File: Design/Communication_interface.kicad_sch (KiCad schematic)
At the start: 6 parts

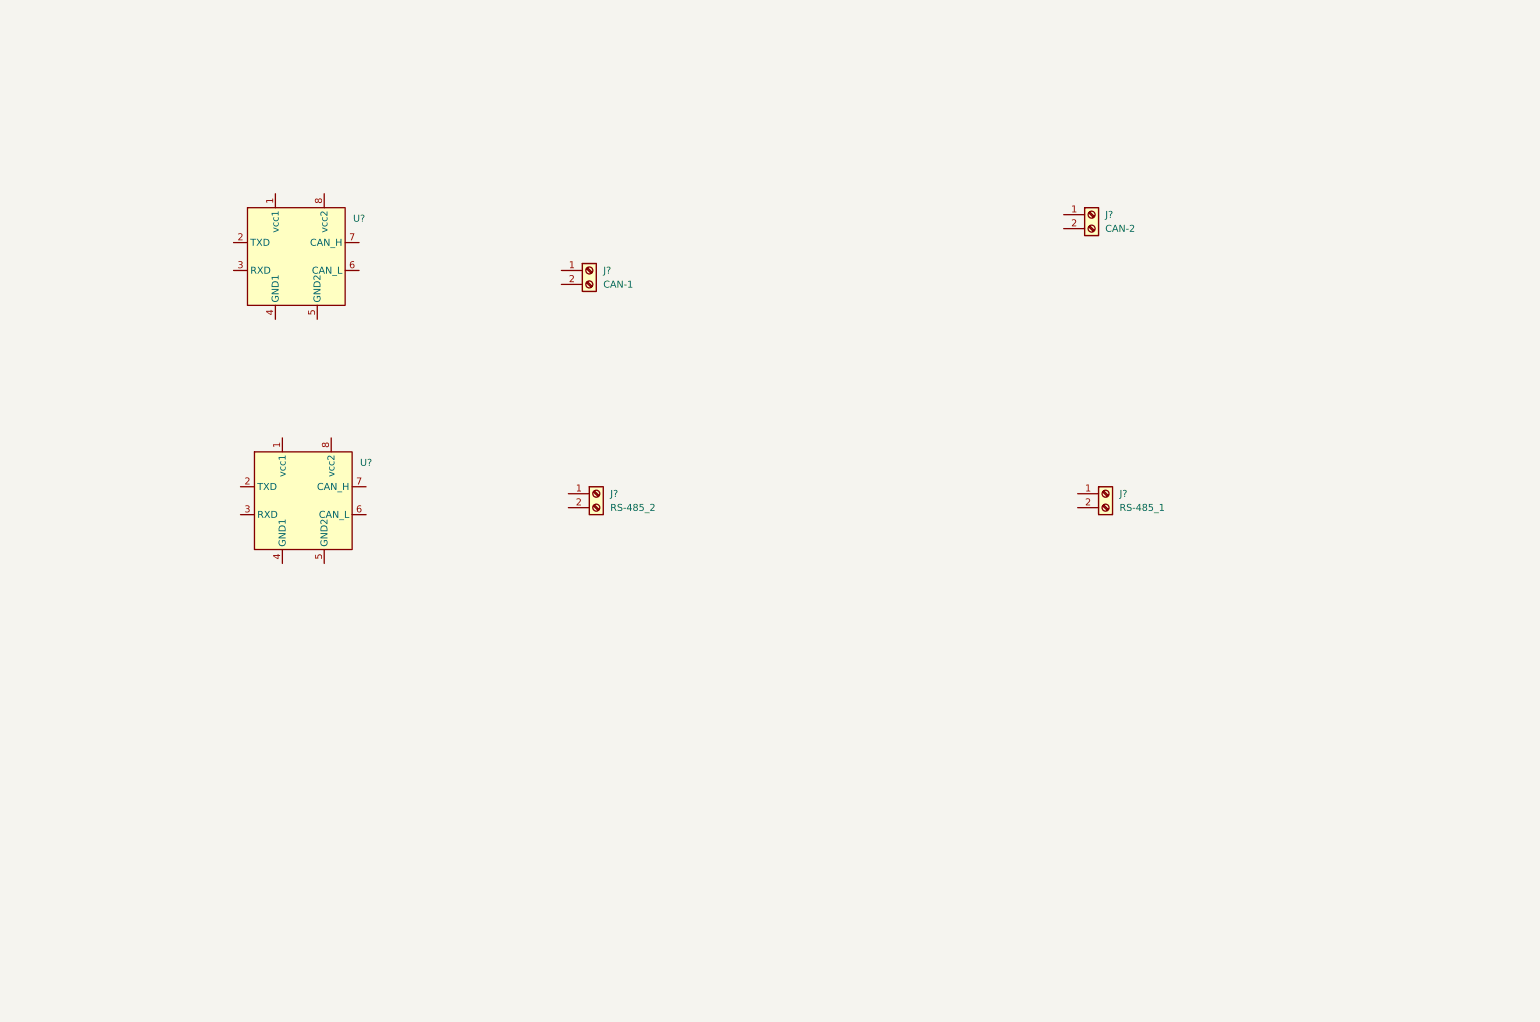
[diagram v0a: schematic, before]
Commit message: Added Comps in Communication.sch
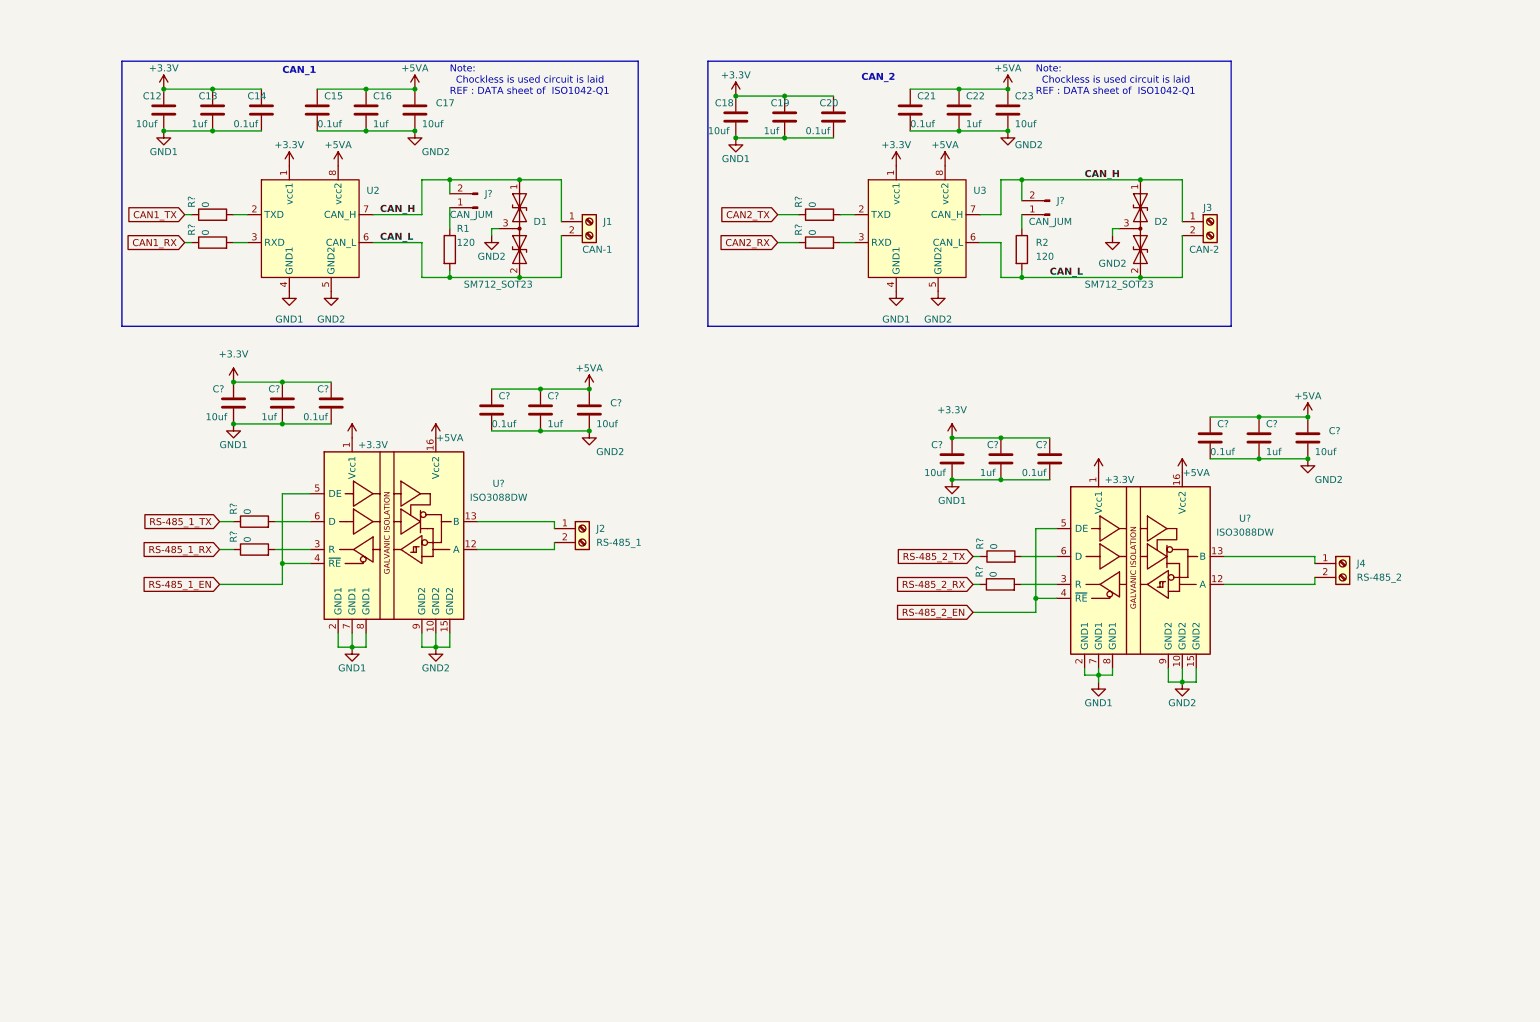
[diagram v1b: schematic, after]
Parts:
- added C12, C17, C18, C23, C? (x4): 10uf, symbol Device:C
- added C13, C16, C19, C22, C? (x4): 1uf, symbol Device:C
- added C14, C15, C20, C21, C? (x4): 0.1uf, symbol Device:C
- added D1, D2: SM712_SOT23, Package_TO_SOT_SMD:SOT-23, symbol Diode:SM712_SOT23
- added J? (x2): CAN_JUM, symbol Connector:Conn_01x02_Pin
- added R1, R2: 120, symbol Device:R
- added R? (x8): 0, symbol Device:R
- added U? (x2): ISO3088DW, Package_SO:SOIC-16W_7.5x10.3mm_P1.27mm, symbol Interface_UART:ISO3088DW
- gave numbers to parts that had none: 6
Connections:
- net CAN_H: now reaches J1.1 (Pin_1)
- net CAN_H: now also J3.1 (Pin_1), U2.7 (CAN_H), U3.7 (CAN_H), D1.1 (A1), D2.1 (A1), J?.2 (Pin_2), J?.2 (Pin_2)
- net CAN_L: now reaches J1.2 (Pin_2)
- net CAN_L: now also J3.2 (Pin_2), U2.6 (CAN_L), U3.6 (CAN_L), D1.2 (A2), D2.2 (A2), R1.2, R2.2
- net +3.3V: now reaches U2.1 (vcc1)
- net +3.3V: now also U3.1 (vcc1), C12.1, C13.1, C14.2, C18.1, C19.1, C20.2, C?.1, C?.1, C?.1, C?.1, C?.2, C?.2, U?.1 (Vcc1), U?.1 (Vcc1)
- net at U2.2 (TXD): now also R?.2
- net at U2.3 (RXD): now also R?.2
- net GND1: now reaches U2.4 (GND1)
- net GND1: now also U3.4 (GND1), C12.2, C13.2, C14.1, C18.2, C19.2, C20.1, C?.1, C?.1, C?.2, C?.2, C?.2, C?.2, U?.2 (GND1), U?.2 (GND1), U?.7 (GND1), U?.7 (GND1), U?.8 (GND1), U?.8 (GND1)
- net GND2: now reaches U2.5 (GND2)
- net GND2: now also U3.5 (GND2), C15.2, C16.2, C17.1, C21.2, C22.2, C23.1, C?.1, C?.1, C?.2, C?.2, C?.2, C?.2, D1.3 (common), D2.3 (common), U?.10 (GND2), U?.10 (GND2), U?.15 (GND2), U?.15 (GND2), U?.9 (GND2), U?.9 (GND2)
- net +5VA: now reaches U2.8 (vcc2)
- net +5VA: now also U3.8 (vcc2), C15.1, C16.1, C17.2, C21.1, C22.1, C23.2, C?.1, C?.1, C?.1, C?.1, C?.2, C?.2, U?.16 (Vcc2), U?.16 (Vcc2)
- net at U3.2 (TXD): now also R?.2
- net at U3.3 (RXD): now also R?.2
- net at J4.1 (Pin_1): now also U?.13 (B)
- net at J4.2 (Pin_2): now also U?.12 (A)
- net at J2.1 (Pin_1): now also U?.13 (B)
- net at J2.2 (Pin_2): now also U?.12 (A)
- new net: J?.1 (Pin_1), R2.1
- new net: R?.2, U?.3 (R) (x2)
- new net: R?.2, U?.6 (D) (x2)
- new net: J?.1 (Pin_1), R1.1
- new net CAN1_RX: R?.1
- new net CAN1_TX: R?.1
- new net CAN2_RX: R?.1
- new net CAN2_TX: R?.1
- new net RS-485_1_EN: U?.4 (~{RE}), U?.5 (DE)
- new net RS-485_1_RX: R?.1
- new net RS-485_1_TX: R?.1
- new net RS-485_2_EN: U?.4 (~{RE}), U?.5 (DE)
- new net RS-485_2_RX: R?.1
- new net RS-485_2_TX: R?.1
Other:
- note added: "CAN_1"
- note added: "CAN_2"
- note added: "Note: Chockless is used circuit is laid REF : DATA sheet of ISO1042-Q1"
- moved on the sheet: J1, J2, J3, J4, U2, U3

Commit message: Added reference file for chokless CAN and DC-DC converter in main sch
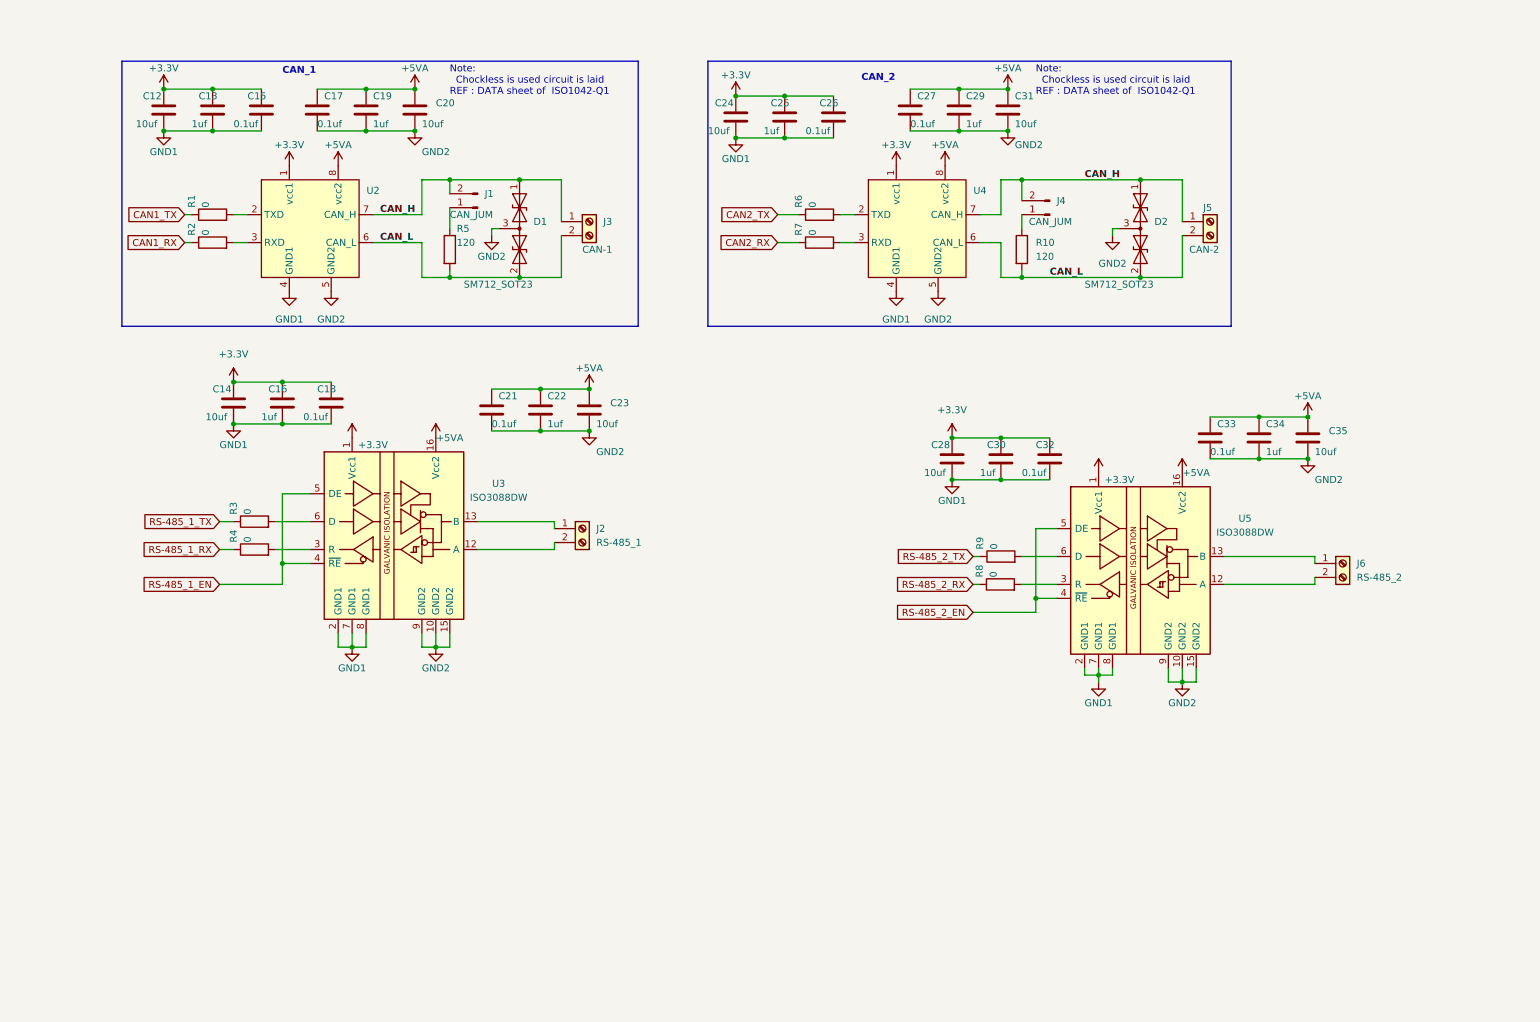
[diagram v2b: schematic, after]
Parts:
- gave numbers to parts that had none: 24
- renumbered C14 to C15, C15 to C17, C16 to C19, C17 to C20, C18 to C24, C19 to C25, C20 to C26, C21 to C27, C22 to C29, C23 to C31, J1 to J3, J3 to J5, J4 to J6, R2 to R10, R1 to R5, U3 to U4

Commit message: Communication.sch modified , 75% finished
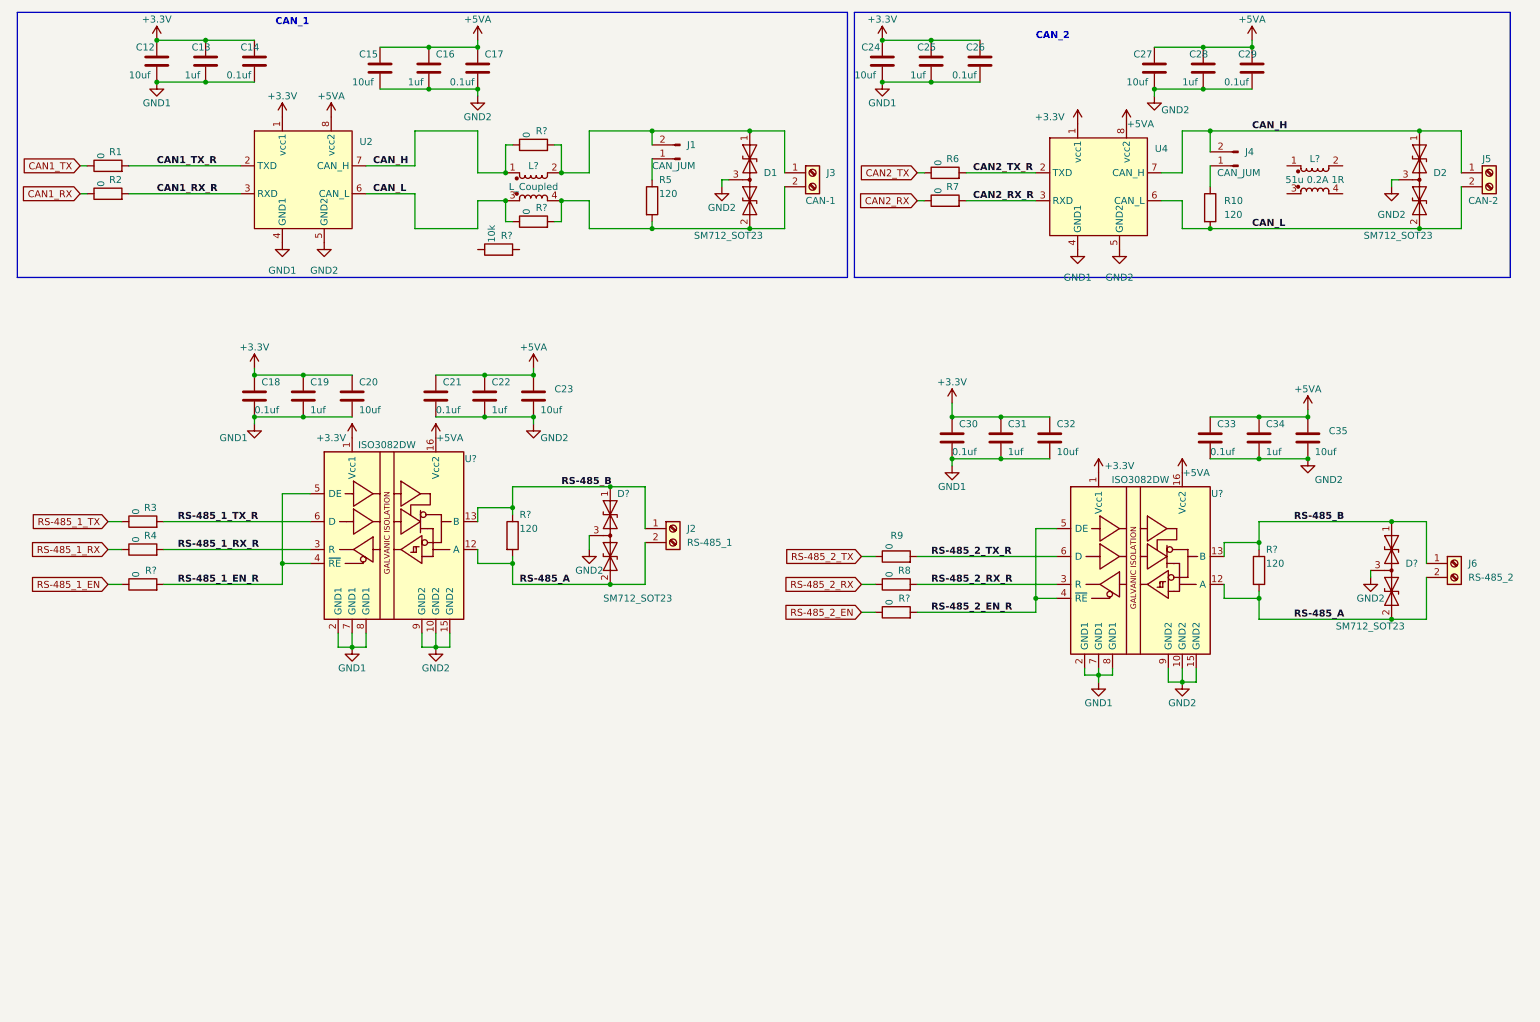
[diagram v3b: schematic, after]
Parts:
- removed U3, U5: ISO3088DW, Package_SO:SOIC-16W_7.5x10.3mm_P1.27mm, symbol Interface_UART:ISO3088DW
- added D? (x2): SM712_SOT23, Package_TO_SOT_SMD:SOT-23, symbol Diode:SM712_SOT23
- added L?: L_Coupled, symbol Device:L_Coupled
- added L?: 51u 0.2A 1R, symbol Device:L_Coupled
- added R? (x2): 120, symbol Device:R
- added R? (x4): 0, symbol Device:R
- added R?: 10k, symbol Device:R
- added U? (x2): ISO3082DW, Package_SO:SOIC-16W_7.5x10.3mm_P1.27mm, symbol Interface_UART:ISO3082DW
- renumbered C15 to C14, C14 to C15, C18 to C17, C17 to C18, C28 to C27, C30 to C28, C32 to C29, C27 to C30, C29 to C31, C31 to C32
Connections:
- net +3.3V: now also C18.1, C19.1, C20.2, C30.1, C31.1, C32.2, U?.1 (Vcc1), U?.1 (Vcc1); no longer C15.1, C16.1, C17.2, C27.1, C28.1, C29.2
- net +5VA: now also C15.1, C16.1, C17.2, C27.1, C28.1, C29.2, U?.16 (Vcc2), U?.16 (Vcc2); no longer C18.1, C19.1, C20.2, C30.1, C31.1, C32.2
- net CAN_H: now also L?.1, R?.1; no longer D1.1 (A1), J1.2 (Pin_2), J3.1 (Pin_1)
- net CAN_L: now also L?.3, R?.1; no longer D1.2 (A2), J3.2 (Pin_2), R5.2
- net GND1: now also C18.2, C19.2, C20.1, C30.2, C31.2, C32.1, U?.2 (GND1), U?.2 (GND1), U?.7 (GND1), U?.7 (GND1), U?.8 (GND1), U?.8 (GND1); no longer C15.2, C16.2, C17.1, C27.2, C28.2, C29.1
- net GND2: now also C15.2, C16.2, C17.1, C27.2, C28.2, C29.1, D?.3 (common), D?.3 (common), U?.10 (GND2), U?.10 (GND2), U?.15 (GND2), U?.15 (GND2), U?.9 (GND2), U?.9 (GND2); no longer C18.2, C19.2, C20.1, C30.2, C31.2, C32.1
- net RS-485_1_EN: now also R?.1
- net RS-485_2_EN: now also R?.1
- net RS-485_2_RX_R: now reaches R8.2
- net RS-485_2_RX_R: now also U?.3 (R)
- net CAN1_RX_R: now reaches R2.2, U2.3 (RXD)
- net RS-485_1_TX_R: now reaches R3.2
- net RS-485_1_TX_R: now also U?.6 (D)
- net RS-485_A: now reaches J6.2 (Pin_2)
- net RS-485_A: now also J2.2 (Pin_2), D?.2 (A2), D?.2 (A2), R?.2, R?.2, U?.12 (A), U?.12 (A)
- net RS-485_B: now reaches J6.1 (Pin_1)
- net RS-485_B: now also J2.1 (Pin_1), D?.1 (A1), D?.1 (A1), R?.1, R?.1, U?.13 (B), U?.13 (B)
- net RS-485_2_TX_R: now reaches R9.2
- net RS-485_2_TX_R: now also U?.6 (D)
- net CAN2_TX_R: now reaches R6.2, U4.2 (TXD)
- net CAN1_TX_R: now reaches R1.2, U2.2 (TXD)
- net CAN2_RX_R: now reaches R7.2, U4.3 (RXD)
- net RS-485_1_RX_R: now reaches R4.2
- net RS-485_1_RX_R: now also U?.3 (R)
- new net: D1.1 (A1), J1.2 (Pin_2), J3.1 (Pin_1), L?.2, R?.2
- new net: D1.2 (A2), J3.2 (Pin_2), L?.4, R5.2, R?.2
- new net RS-485_1_EN_R: R?.2, U?.4 (~{RE}), U?.5 (DE)
- new net RS-485_2_EN_R: R?.2, U?.4 (~{RE}), U?.5 (DE)
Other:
- note removed: "Note: Chockless is used circuit is laid REF : DATA sheet of ISO1042-Q1"
- moved on the sheet: C12, C13, C14, C15, C16, C17, C18, C19, C20, C21, C22, C23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

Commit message: Added HUM and TEMP sense
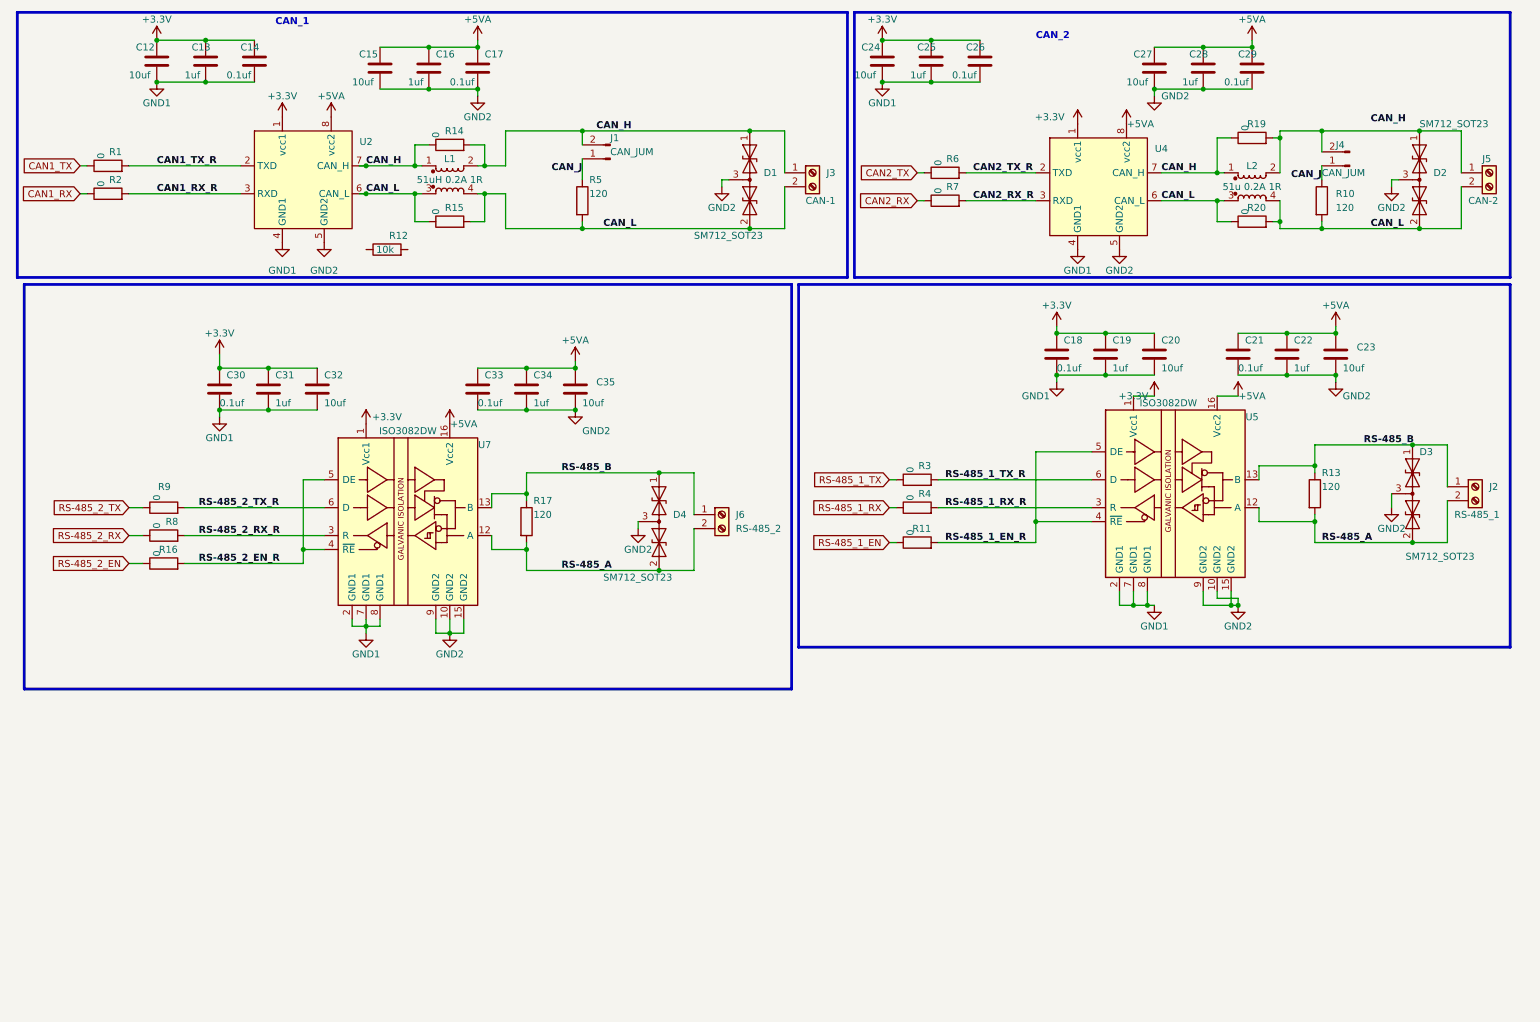
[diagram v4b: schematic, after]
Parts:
- added R19, R20: 0, symbol Device:R
- L1: renamed from L?; value L_Coupled -> 51uH 0.2A 1R
- gave numbers to parts that had none: 12
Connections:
- net CAN_H: now also D1.1 (A1), J1.2 (Pin_2), J3.1 (Pin_1), L1.2, L2.1, R14.2, R19.1; no longer D2.1 (A1), J4.2 (Pin_2), J5.1 (Pin_1)
- net CAN_L: now also D1.2 (A2), J3.2 (Pin_2), L1.4, L2.3, L2.4, R15.2, R5.2, R20.1, R20.2
- net CAN_J: now reaches J4.1 (Pin_1), R10.1
- net CAN_J: now also J1.1 (Pin_1), R5.1
- net at L2.2: now also D2.1 (A1), J4.2 (Pin_2), J5.1 (Pin_1), R19.2
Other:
- moved on the sheet: C18, C19, C20, C21, C22, C23, C30, C31, C32, C33, C34, C35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
